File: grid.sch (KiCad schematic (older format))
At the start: 259 parts, among them Q1 BSS83P, Q10 BSS83P, Q11 BSS83P, Q12 BSS83P, Q13 BSS83P, Q14 BSS83P, Q15 BSS83P, Q16 BSS83P, Q17 BSS83P, Q18 BSS83P, Q19 BSS83P, Q2 BSS83P, Q20 BSS83P, Q21 NX7002AK, Q22 NX7002AK, Q23 NX7002AK, Q24 NX7002AK, Q25 NX7002AK, Q26 NX7002AK, Q27 NX7002AK, Q28 NX7002AK, Q29 NX7002AK, Q3 BSS83P, Q30 NX7002AK, Q31 NX7002AK, Q32 NX7002AK, Q4 BSS83P, Q5 BSS83P, Q6 BSS83P, Q7 BSS83P, Q8 BSS83P, Q9 BSS83P, SW1 Button_matrix_4x4, SW10 SW_Push, SW11 SW_Push, SW12 SW_Push, SW13 SW_Push, SW14 SW_Push, SW15 SW_Push, SW16 SW_Push, SW17 SW_Push, SW18 SW_Push, SW19 SW_Push, SW2 Button_matrix_4x4, SW20 SW_Push, SW3 Button_matrix_4x4, SW4 Button_matrix_4x4, SW5 SW_Push, SW6 SW_Push, SW7 SW_Push, SW8 SW_Push, SW9 SW_Push, U1 74HC138, U2 74HC138, U3 74HC138

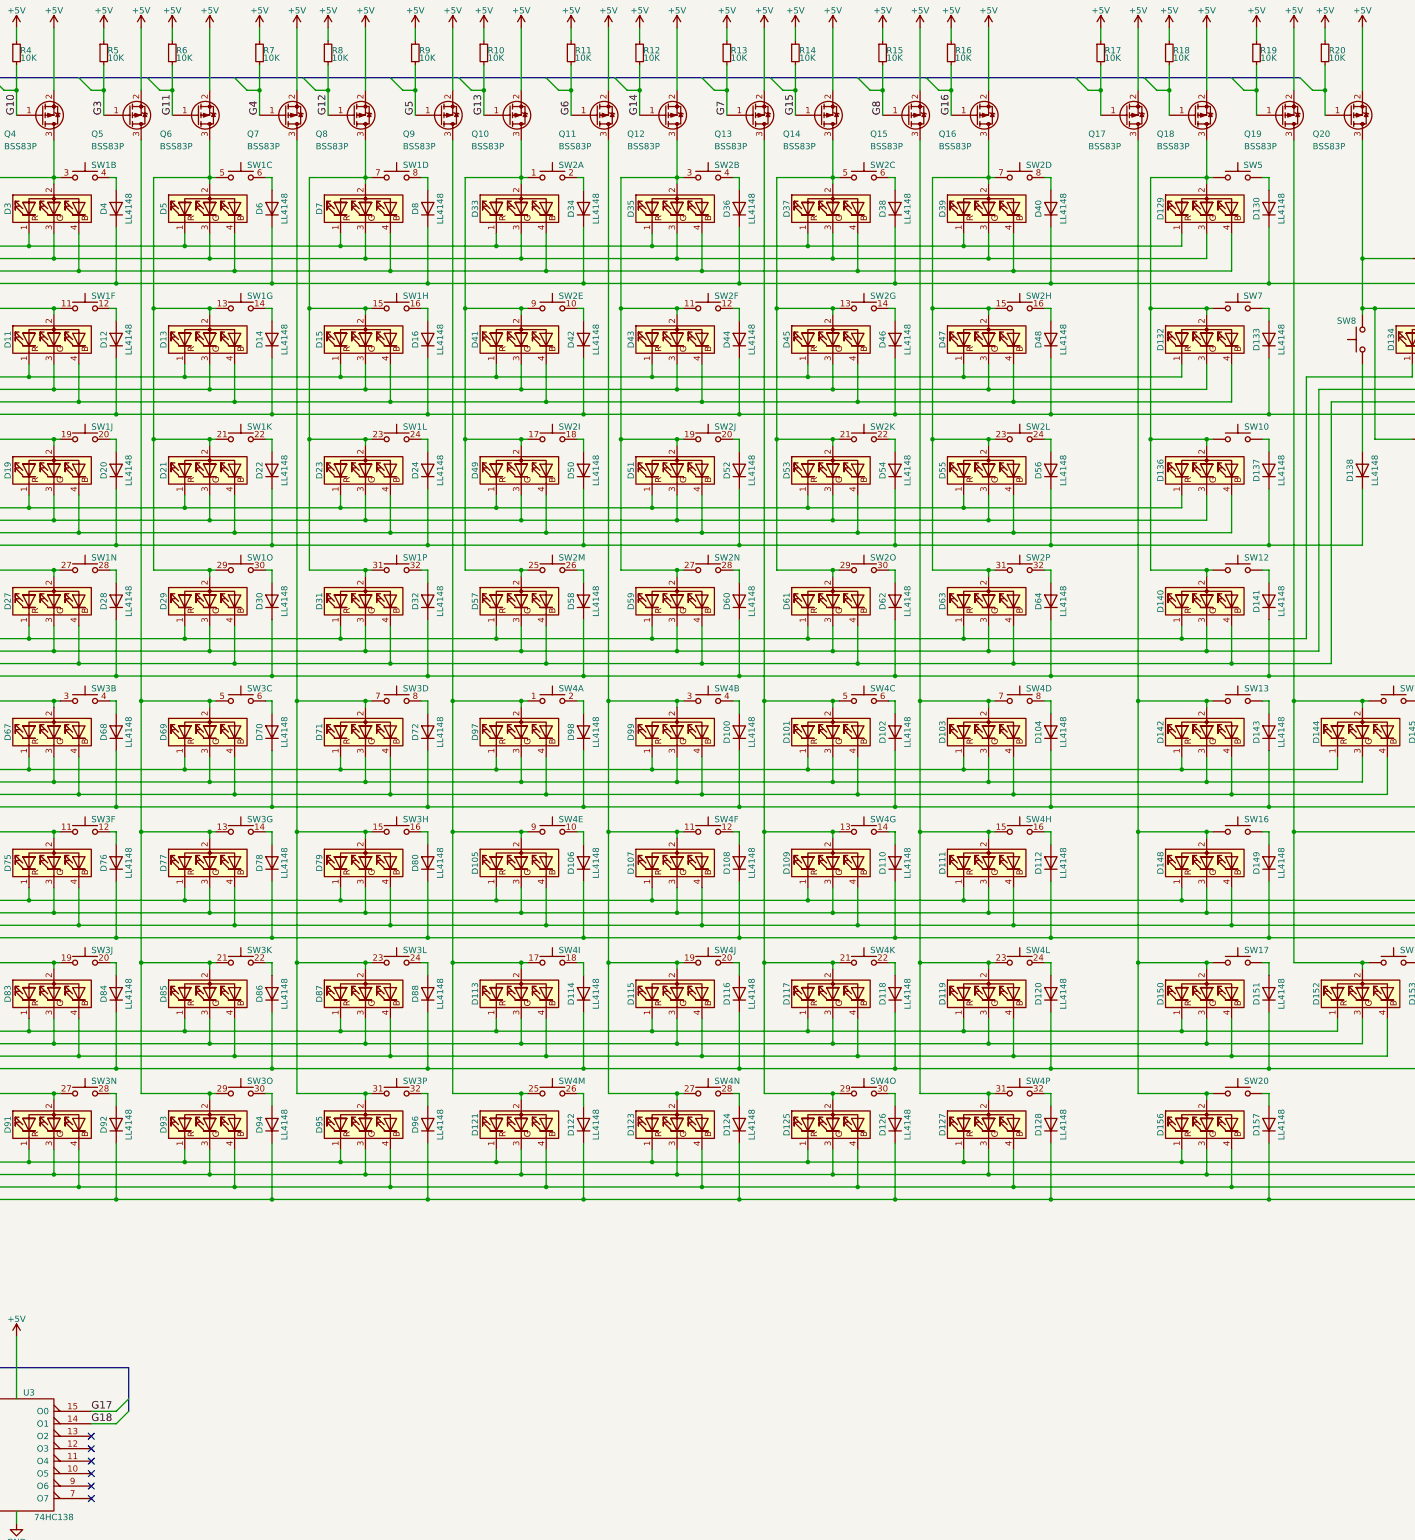
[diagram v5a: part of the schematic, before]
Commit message: added net names in grid schematic
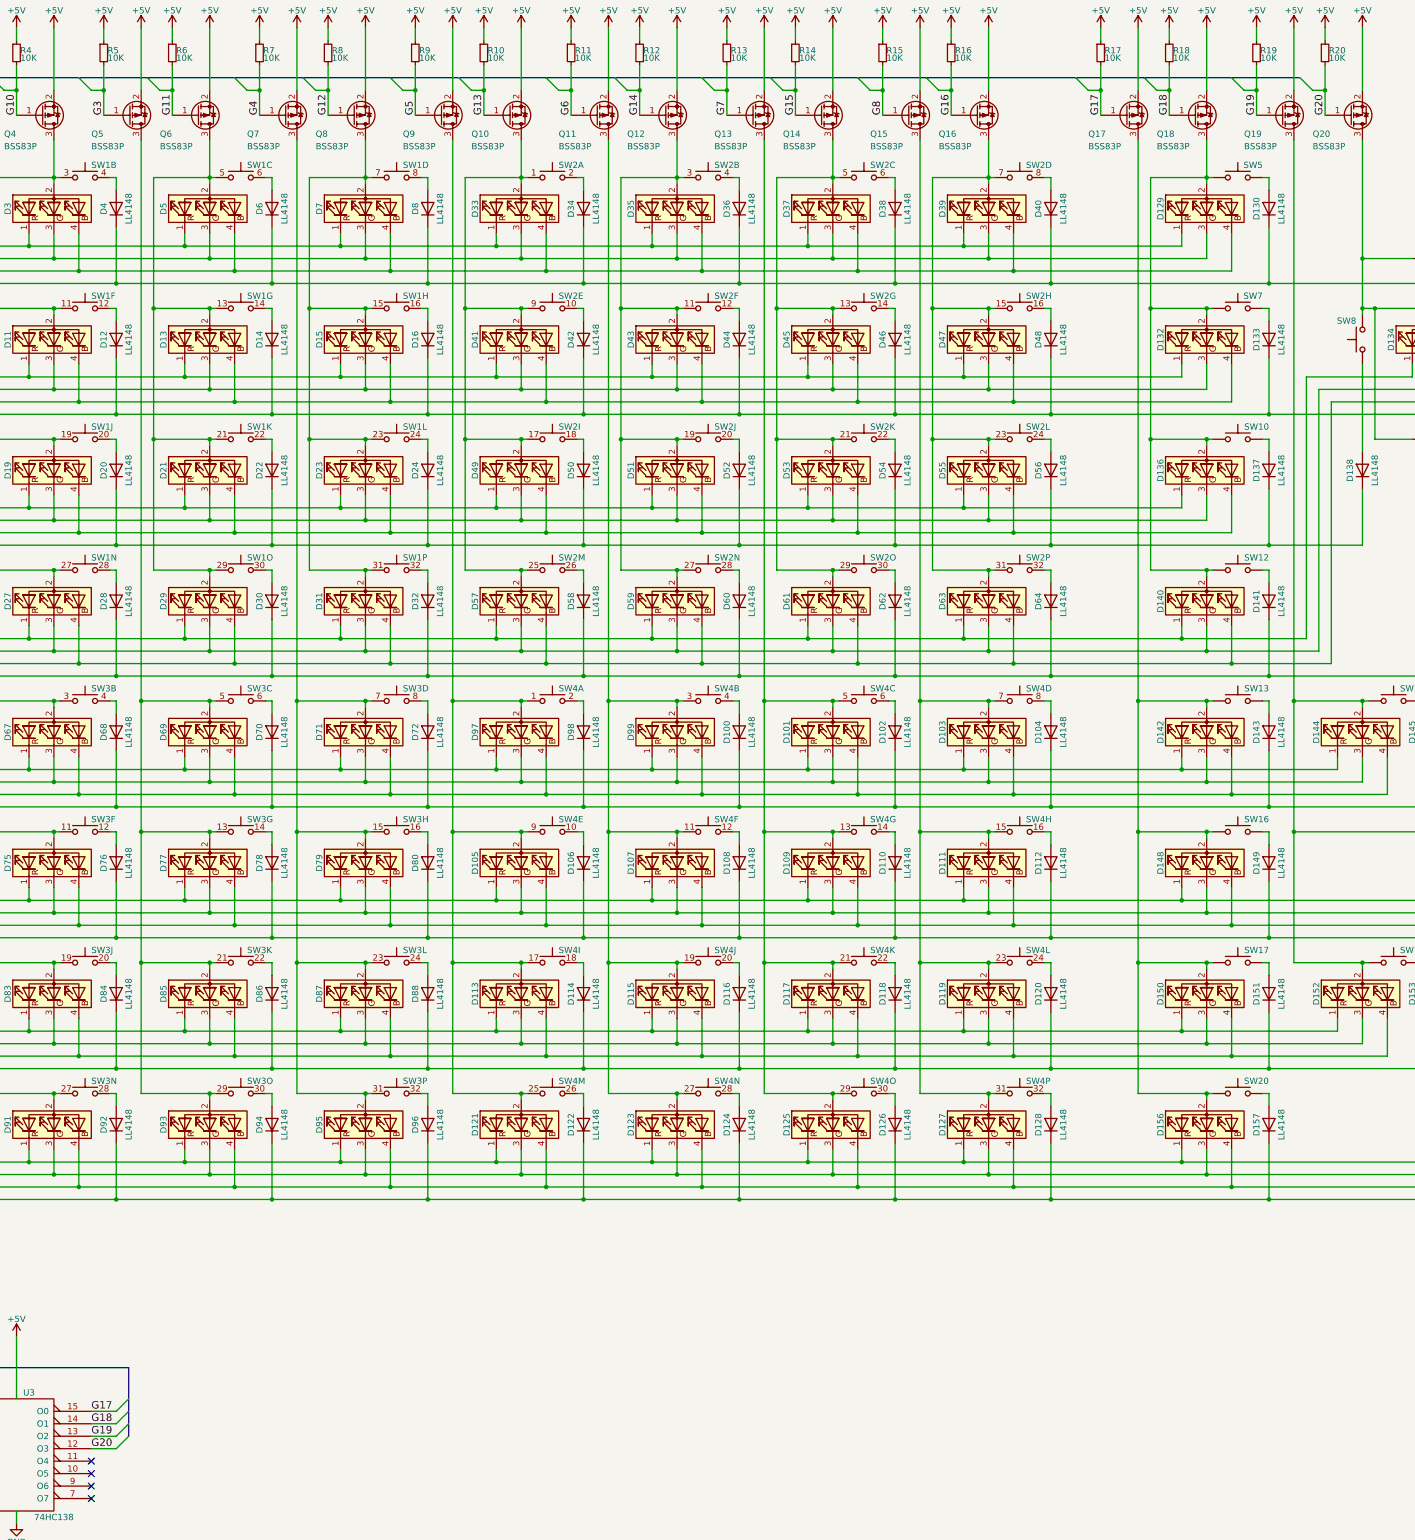
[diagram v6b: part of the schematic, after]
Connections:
- net G17: now also Q17.1 (G), R17.2
- net G18: now also Q18.1 (G), R18.2
- net G20: now reaches U3.12 (O3)
- net G20: now also Q20.1 (G), R20.2
- net G19: now reaches U3.13 (O2)
- net G19: now also Q19.1 (G), R19.2
- no-connect marks 6 -> 4
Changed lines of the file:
@@
 	1    0    0    -1
 $EndComp
-NoConn ~ 9850 13350
-NoConn ~ 9850 13450
 NoConn ~ 9850 13550
 NoConn ~ 9850 13650
@@
 Connection ~ 7850 12800
 Wire Bus Line
-	10150 12800 10150 13150
+	10150 12800 10150 13350
 Wire Wire Line
 	18350 3250 18850 3250
@@
 Wire Wire Line
 	21600 3900 21500 3900
+Text Label 17950 2750 1    60   ~ 0
+G17
+Text Label 18500 2750 1    60   ~ 0
+G18
+Text Label 19200 2750 1    60   ~ 0
+G19
+Text Label 19750 2750 1    60   ~ 0
+G20
+Text Label 9850 13350 0    60   ~ 0
+G19
+Text Label 9850 13450 0    60   ~ 0
+G20
+Wire Wire Line
+	9850 13350 10050 13350
+Wire Wire Line
+	9850 13450 10050 13450
+Entry Wire Line
+	10050 13350 10150 13250
+Entry Wire Line
+	10050 13450 10150 13350
 $EndSCHEMATC
